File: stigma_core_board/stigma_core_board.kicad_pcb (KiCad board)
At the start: 4 copper layers, 40 x 40 mm, 93 parts, among them J1 TC2050, J5 USB_C_Receptacle_USB2.0, SW1 KMR721NGLFS, SW2 KMR721NGLFS, U1 STM32H743VITx, U10 H3LIS331DL, U11 MS5607/MS5611, U12 LIS3MDL, U13 BMP580/BMP388/LPS22, U2 TPD4E1U06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

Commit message: Update LCSC references
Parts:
- D4: footprint Diode_SMD:D_SOD-123F -> Diode_SMD:D_SOD-123
- U13: value BMP580/BMP388/LPS22 -> BMP580
- U3: value BMP580/BMP388/LPS22 -> LPS22
- U6: value ICM-42688 (or other LGA-14 IMU) -> ICM-42688-P
- moved D4 0.25 mm to (126.2, 109.8)

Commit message: Tweak routing
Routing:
- net GND: track 112.1 -> 124.4 mm, vias 195 -> 202
- net SWDIO: track 12.1 -> 17.4 mm
- net PC1_ETH_MDC: track 8.57 -> 11.6 mm
- net PA3: track 7.15 -> 10.2 mm
- net Net-(J1-Pin_2): track 24.8 -> 27.7 mm
- net PA2_ETH_MDIO: track 9.07 -> 11.2 mm
- net PE2: track 16.9 -> 15.2 mm
- net PA1_ETH_REF_CLK: track 8.57 -> 10.2 mm
- net PA0: track 8.47 -> 9.84 mm
- net PA7_ETH_CRS_DV: track 12.5 -> 11.6 mm
- net PB1: track 15.6 -> 14.7 mm
- net ETH_RXD+: track 11.6 -> 10.9 mm
- net ETH_RXD-: track 11.5 -> 10.8 mm
- net Net-(J5-CC1): track 7.58 -> 8.10 mm

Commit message: Minor layout tweaks
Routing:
- net +5V: track 84.9 -> 85.8 mm
- net PC1_ETH_MDC: track 11.6 -> 10.9 mm
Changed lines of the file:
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@@
 	)
 	(segment
+		(start 113.2 124.85)
+		(end 114.05 124.85)
+		(width 0.5)
+		(layer "F.Cu")
+		(net 11)
+	)
+	(segment
 		(start 125.85 130.95)
 		(end 126.15 130.95)
@@
 	(segment
 		(start 113.2 124.85)
-		(end 114.05 124.85)
-		(width 0.5)
-		(layer "F.Cu")
-		(net 11)
-	)
-	(segment
-		(start 113.2 124.85)
 		(end 112.875 125.175)
 		(width 0.5)
@@
 	)
 	(segment
+		(start 114.05 124.85)
+		(end 113.2 124.85)
+		(width 0.5)
+		(layer "B.Cu")
+		(net 11)
+	)
+	(segment
 		(start 106.45 121.88)
 		(end 106.45 119.3)
@@
 	)
 	(segment
-		(start 108.724999 115.833299)
-		(end 108.682689 115.833299)
+		(start 108.720327 115.795661)
+		(end 108.265988 116.25)
 		(width 0.2)
 		(layer "F.Cu")
@@
 	)
 	(segment
-		(start 108.682689 115.833299)
-		(end 108.265988 116.25)
+		(start 109.062003 115.795661)
+		(end 108.720327 115.795661)
 		(width 0.2)
 		(layer "F.Cu")
@@
 	)
 	(via
-		(at 108.724999 115.833299)
+		(at 109.062003 115.795661)
 		(size 0.5)
 		(drill 0.25)
@@
 	)
 	(segment
-		(start 108.724999 115.833299)
-		(end 109.188305 115.833299)
+		(start 109.150667 115.795661)
+		(end 109.65 116.294994)
 		(width 0.2)
 		(layer "B.Cu")
@@
 	)
 	(segment
-		(start 109.188305 115.833299)
-		(end 109.65 116.294994)
+		(start 109.062003 115.795661)
+		(end 109.150667 115.795661)
 		(width 0.2)
 		(layer "B.Cu")
@@
 	)
 	(via
-		(at 109.15 114.638083)
+		(at 109.14 114.54)
 		(size 0.5)
 		(drill 0.25)
@@
 	)
 	(segment
-		(start 109.15 114.305006)
-		(end 109.25 114.205006)
-		(width 0.2)
-		(layer "B.Cu")
-		(net 88)
-	)
-	(segment
 		(start 112.018146 115.031408)
 		(end 112.05 114.999554)
@@
 	)
 	(segment
-		(start 109.25 114.205006)
-		(end 109.25 113.89)
-		(width 0.2)
-		(layer "B.Cu")
-		(net 88)
-	)
-	(segment
 		(start 118.85 113.4)
 		(end 118.6 113.15)
@@
 	)
 	(segment
-		(start 109.15 114.638083)
-		(end 109.15 114.305006)
+		(start 118.6 113.15)
+		(end 118.25 113.15)
 		(width 0.2)
 		(layer "B.Cu")
@@
 	)
 	(segment
-		(start 118.6 113.15)
-		(end 118.25 113.15)
+		(start 115.25 113.231801)
+		(end 115.25 113.89)
 		(width 0.2)
 		(layer "B.Cu")
@@
 	)
 	(segment
-		(start 115.25 113.231801)
-		(end 115.25 113.89)
+		(start 109.14 114.315006)
+		(end 109.25 114.205006)
 		(width 0.2)
 		(layer "B.Cu")
@@
 	)
 	(segment
+		(start 109.14 114.54)
+		(end 109.14 114.315006)
+		(width 0.2)
+		(layer "B.Cu")
+		(net 88)
+	)
+	(segment
 		(start 111.958462 115.031408)
 		(end 111.613873 114.686819)
@@
 	)
 	(segment
+		(start 109.25 114.205006)
+		(end 109.25 113.89)
+		(width 0.2)
+		(layer "B.Cu")
+		(net 88)
+	)
+	(segment
 		(start 121.25 113.517618)
 		(end 121.25 113.89)
@@
 	)
 	(segment
-		(start 109.6 115.8)
-		(end 109.6 115.901472)
+		(start 108.990736 116.245661)
+		(end 108.486397 116.75)
 		(width 0.2)
 		(layer "F.Cu")
@@
 	)
 	(segment
-		(start 109.48 113.79)
-		(end 108.84 113.79)
+		(start 109.27 115.28)
+		(end 109.48 115.28)
 		(width 0.2)
 		(layer "F.Cu")
@@
 	)
 	(segment
-		(start 108.72 113.91)
-		(end 108.72 113.97)
+		(start 109.48 113.79)
+		(end 108.84 113.79)
 		(width 0.2)
 		(layer "F.Cu")
@@
 	)
 	(segment
-		(start 108.93 115.42)
-		(end 109.48 115.42)
+		(start 108.72 113.91)
+		(end 108.72 113.97)
 		(width 0.2)
 		(layer "F.Cu")
@@
 	)
 	(segment
-		(start 108.486397 116.75)
-		(end 107.575 116.75)
+		(start 108.84 114.09)
+		(end 109.48 114.09)
 		(width 0.2)
 		(layer "F.Cu")
@@
 	)
 	(segment
-		(start 108.84 114.09)
-		(end 109.48 114.09)
+		(start 109.6 113.108828)
+		(end 109.6 113.67)
 		(width 0.2)
 		(layer "F.Cu")
@@
 	)
 	(segment
-		(start 109.6 115.901472)
-		(end 109.255811 116.245661)
+		(start 109.6 114.27)
+		(end 109.6 114.3)
 		(width 0.2)
 		(layer "F.Cu")
@@
 	)
 	(segment
-		(start 109.255811 116.245661)
-		(end 108.990736 116.245661)
+		(start 109.583123 113.091951)
+		(end 109.6 113.108828)
 		(width 0.2)
 		(layer "F.Cu")
@@
 	)
 	(segment
-		(start 109.6 113.108828)
-		(end 109.6 113.67)
+		(start 109.6 115.46)
+		(end 109.6 115.8)
 		(width 0.2)
 		(layer "F.Cu")
@@
 	)
 	(segment
-		(start 109.6 114.3)
-		(end 109.6 115)
+		(start 109.6 115.8)
+		(end 109.6 115.901472)
 		(width 0.2)
 		(layer "F.Cu")
@@
 	)
 	(segment
-		(start 109.6 114.27)
-		(end 109.6 114.3)
+		(start 109.6 114.21)
+		(end 109.6 114.27)
 		(width 0.2)
 		(layer "F.Cu")
@@
 	)
 	(segment
-		(start 109.583123 113.091951)
-		(end 109.6 113.108828)
+		(start 109.6 115.901472)
+		(end 109.255811 116.245661)
 		(width 0.2)
 		(layer "F.Cu")
@@
 	)
 	(segment
-		(start 109.48 115.12)
-		(end 108.93 115.12)
+		(start 109.15 115.1)
+		(end 109.15 115.16)
 		(width 0.2)
 		(layer "F.Cu")
@@
 	)
 	(segment
-		(start 108.990736 116.245661)
-		(end 108.486397 116.75)
+		(start 109.48 114.98)
+		(end 109.27 114.98)
 		(width 0.2)
 		(layer "F.Cu")
@@
 	)
 	(segment
-		(start 109.6 114.21)
-		(end 109.6 114.27)
+		(start 109.6 114.3)
+		(end 109.6 114.86)
 		(width 0.2)
 		(layer "F.Cu")
@@
 	)
 	(segment
-		(start 109.6 115.6)
-		(end 109.6 115.8)
+		(start 109.6 115.4)
+		(end 109.6 115.46)
 		(width 0.2)
 		(layer "F.Cu")
@@
 	)
 	(segment
-		(start 109.6 115.54)
-		(end 109.6 115.6)
+		(start 108.486397 116.75)
+		(end 107.575 116.75)
 		(width 0.2)
 		(layer "F.Cu")
@@
 	)
 	(segment
-		(start 108.81 115.24)
-		(end 108.81 115.3)
+		(start 109.255811 116.245661)
+		(end 108.990736 116.245661)
 		(width 0.2)
 		(layer "F.Cu")
@@
 	)
 	(arc
-		(start 108.81 115.3)
-		(mid 108.845147 115.384853)
-		(end 108.93 115.42)
+		(start 109.6 114.86)
+		(mid 109.564853 114.944853)
+		(end 109.48 114.98)
+		(width 0.2)
+		(layer "F.Cu")
+		(net 125)
+	)
+	(arc
+		(start 109.48 115.28)
+		(mid 109.564853 115.315147)
+		(end 109.6 115.4)
 		(width 0.2)
 		(layer "F.Cu")
@@
 	)
 	(arc
-		(start 108.93 115.12)
-		(mid 108.845147 115.155147)
-		(end 108.81 115.24)
+		(start 109.27 114.98)
+		(mid 109.185147 115.015147)
+		(end 109.15 115.1)
+		(width 0.2)
+		(layer "F.Cu")
+		(net 125)
+	)
+	(arc
+		(start 109.15 115.16)
+		(mid 109.185147 115.244853)
+		(end 109.27 115.28)
 		(width 0.2)
 		(layer "F.Cu")
@@
 		(net 125)
 	)
-	(arc
-		(start 109.6 115)
-		(mid 109.564853 115.084853)
-		(end 109.48 115.12)
-		(width 0.2)
-		(layer "F.Cu")
-		(net 125)
-	)
-	(arc
-		(start 109.48 115.42)
-		(mid 109.564853 115.455147)
-		(end 109.6 115.54)
-		(width 0.2)
-		(layer "F.Cu")
-		(net 125)
-	)
 	(segment
 		(start 109.583123 113.091951)
@@
 		(base_line
 			(pts
-				(xy 109.6 115) (xy 109.6 115.8)
+				(xy 109.6 114.86) (xy 109.6 115.8)
 			)
 		)
@@
 		(last_status "tuned")
 		(last_track_width 0.2)
-		(last_tuning "13.0728 mm (tuned)")
-		(max_amplitude 1.04)
+		(last_tuning "12.5132 mm (tuned)")
+		(max_amplitude 0.6)
 		(min_amplitude 0.02)
 		(min_spacing 0.17)
 		(origin
-			(xy 109.6 115)
+			(xy 109.6 114.86)
 		)
 		(override_custom_rules no)
@@
 		(target_skew_min -0.1)
 		(tuning_mode "single")
-		(members 2585e20f-4a8c-478d-8ac4-1149f265714d 3559a627-c0c3-4b64-b16a-5b7b8ac6a93f
-			80fbf513-ff44-4c1f-84ea-3771d7bc1094 91e31208-cc61-4093-8448-1f3f3987d2a7
-			ba443be0-f628-483e-93a6-540849705d64 cb82639a-6d50-4b85-8166-b86fdd5ead69
-			e418a197-abfd-4e90-8c6e-e574207fe112 e46d68df-d1e5-4b40-bb3c-5f89e9fb42ec
-			e6e14e78-9cec-4210-a722-a0c50c543ec3
+		(members 0259e00c-9ed5-4fd1-8282-a53396e8aba6 21b8111f-1cc3-4966-b26e-453f928ff981
+			36fdd3e3-f6ef-481d-a199-ed1790eb7bd5 74bef20d-ed03-483a-9934-713e3eae4cce
+			898c97ab-6e85-4e9c-91ca-d3bfb0b45b93 9700eba5-da46-4409-999c-fde6f670c7de
+			b0942bd4-7091-4582-a69b-6ab1850de12c b61dd31d-4ab2-4ac4-bc0f-979b543bdf15
+			d03feb0c-e362-4b17-8e16-c53f901778ce
 		)
 	)

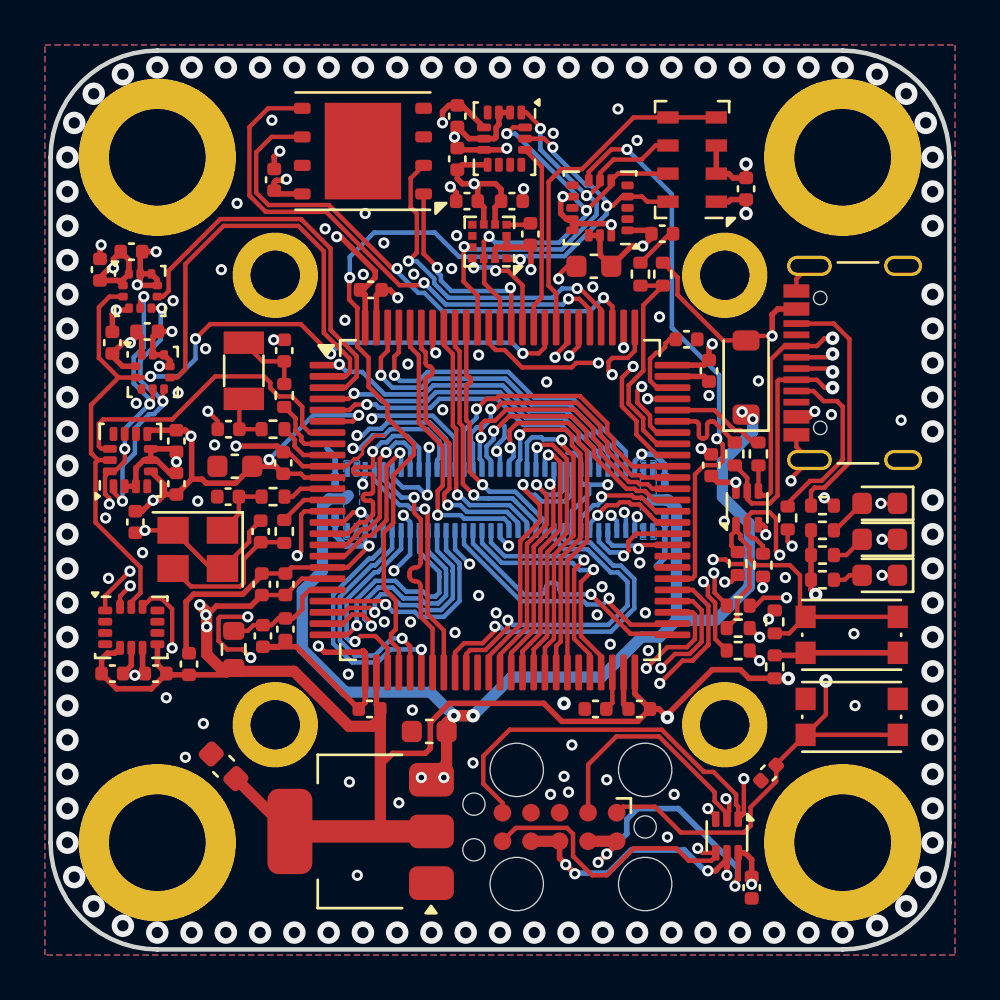
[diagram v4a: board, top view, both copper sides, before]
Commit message: Minor routing tweaks, add net colors
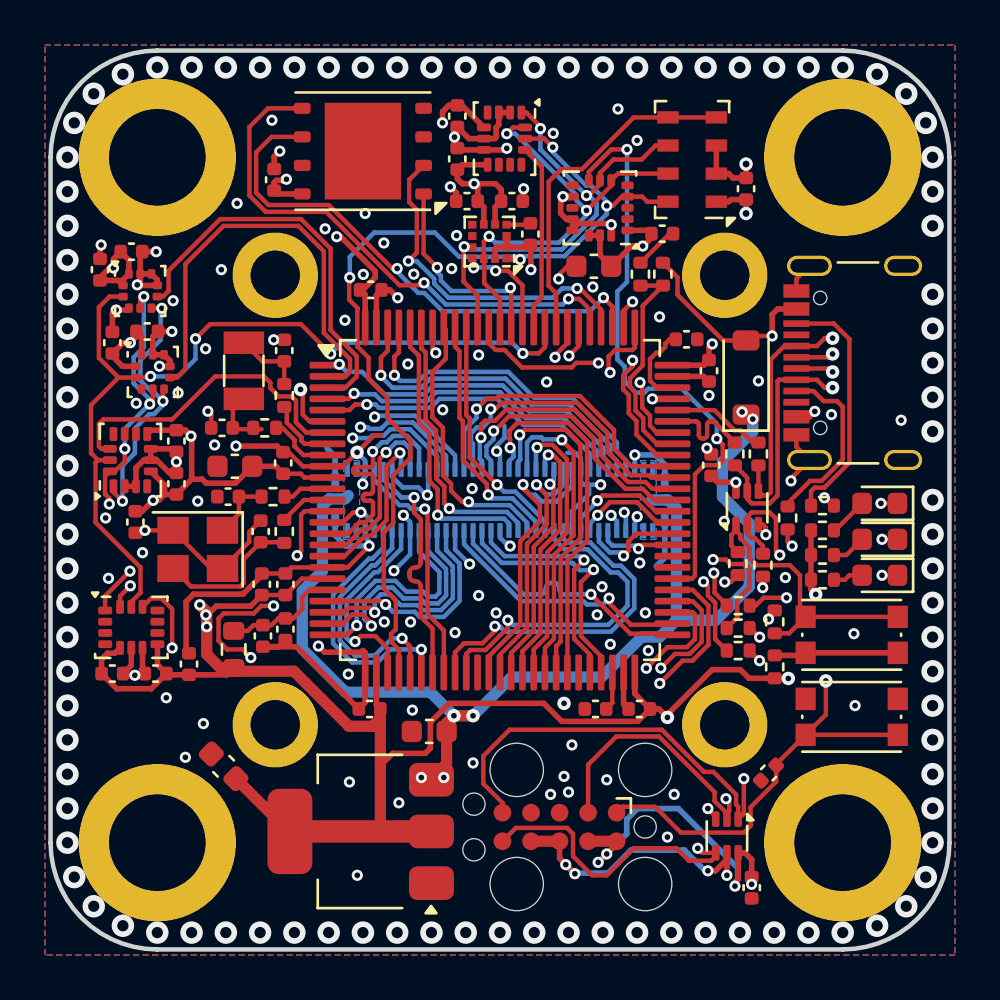
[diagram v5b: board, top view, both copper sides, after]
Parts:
- moved R4 0.37 mm to (104.8, 112.0)
- moved C14 0.30 mm to (102.9, 112.0)
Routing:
- net LED_GREEN: track 26.1 -> 28.1 mm
- net SPI1_CS_HIGHG: track 25.2 -> 27.0 mm
- net SPI3_MOSI: track 45.1 -> 43.9 mm
- net PD1: track 10.9 -> 11.9 mm
- net SPI3_MISO: track 33.8 -> 32.8 mm
- net +3.3V: track 230.4 -> 231.4 mm, vias 23 -> 22
- net GND: track 124.3 -> 123.4 mm, vias 202 -> 203
- net PD0: track 10.5 -> 11.3 mm
- net SPI3_SCK: track 40.3 -> 39.5 mm
- net PB5: track 11.4 -> 10.8 mm
- net PB7: track 11.7 -> 12.2 mm

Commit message: minor changes
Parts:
- U4: value IIM-42652 (or other LGA-14 IMU) -> ICM-42670-P
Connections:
- net Net-(C10-Pad1) renamed /VCAP2
- net Net-(C9-Pad1) renamed /VCAP1
- net Net-(D4-A) renamed /VBUS
- net Net-(J1-Pin_2) renamed /J1-SWDIO
- net Net-(J1-Pin_5) renamed /J1-SWO

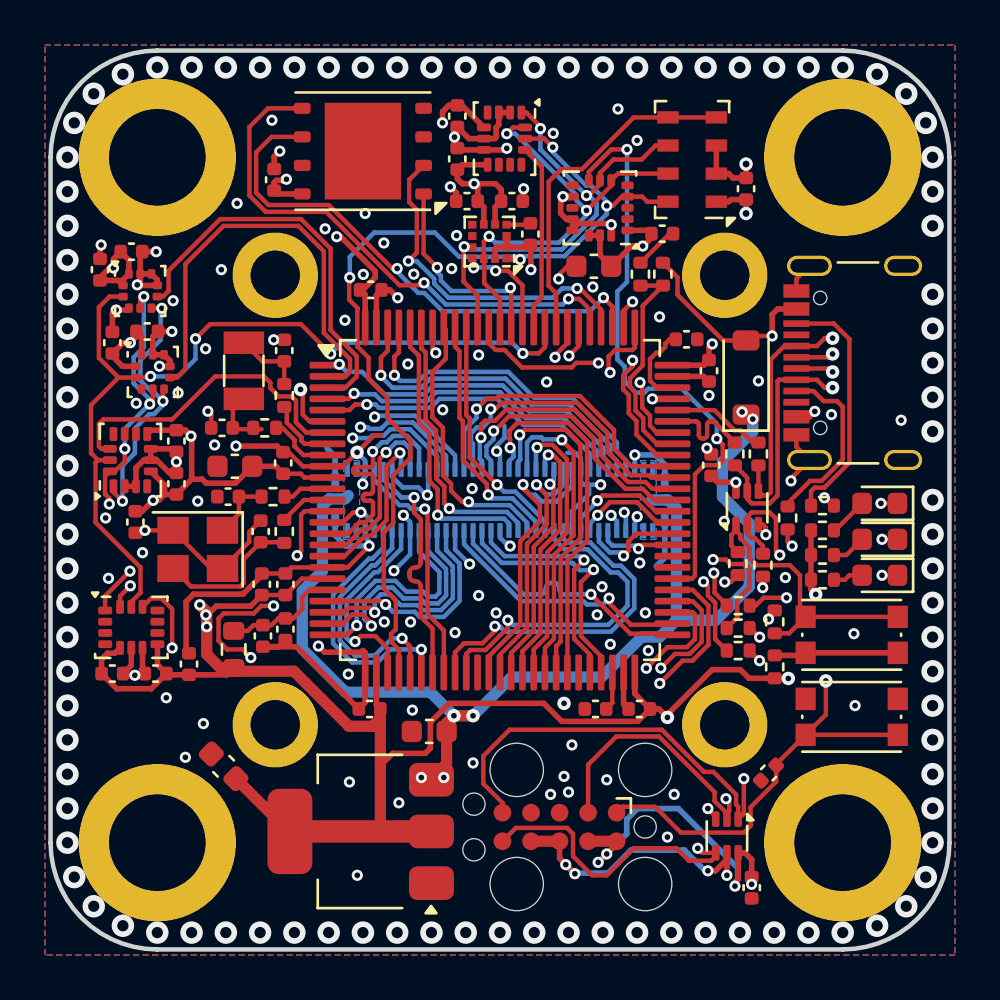
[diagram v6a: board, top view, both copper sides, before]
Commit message: Add correct load capacitors, tweak USB routing, fab options
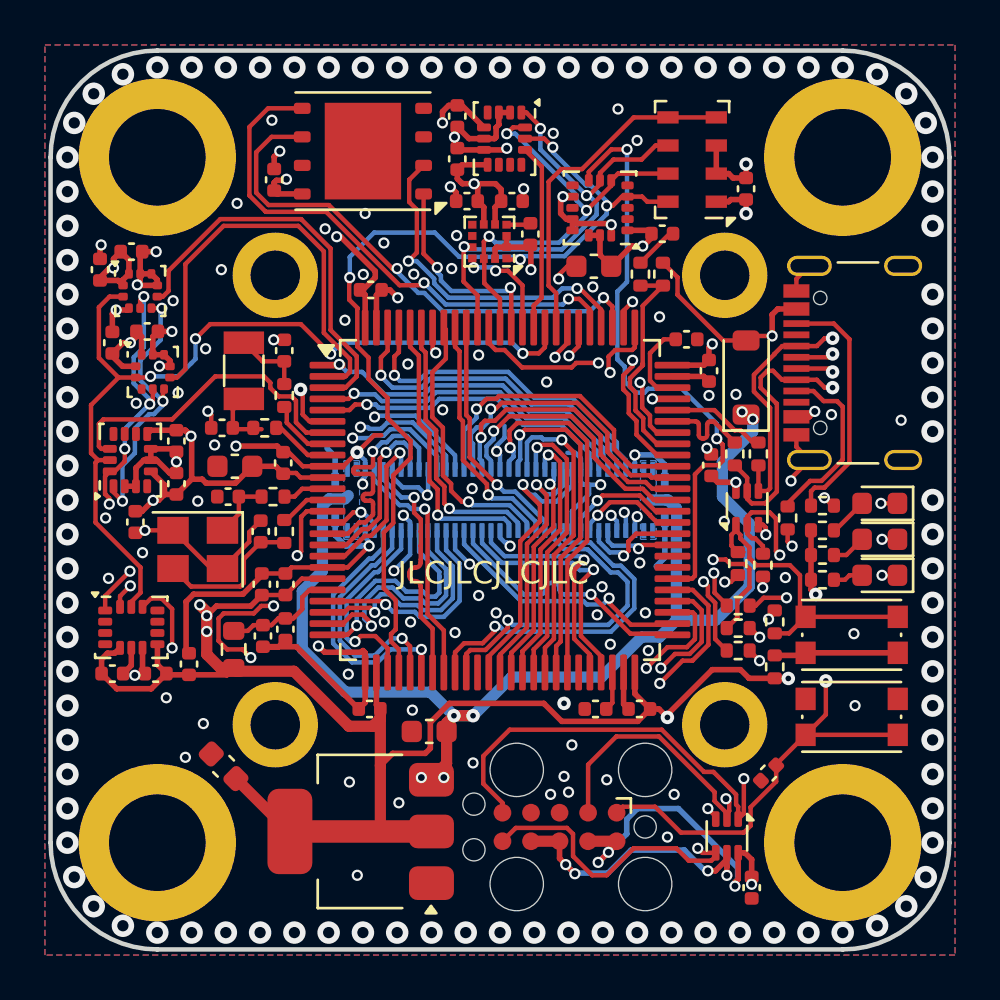
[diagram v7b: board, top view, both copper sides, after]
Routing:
- net /D0-: track 14.6 -> 15.9 mm
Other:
- board text added: "JLCJLCJLCJLC"

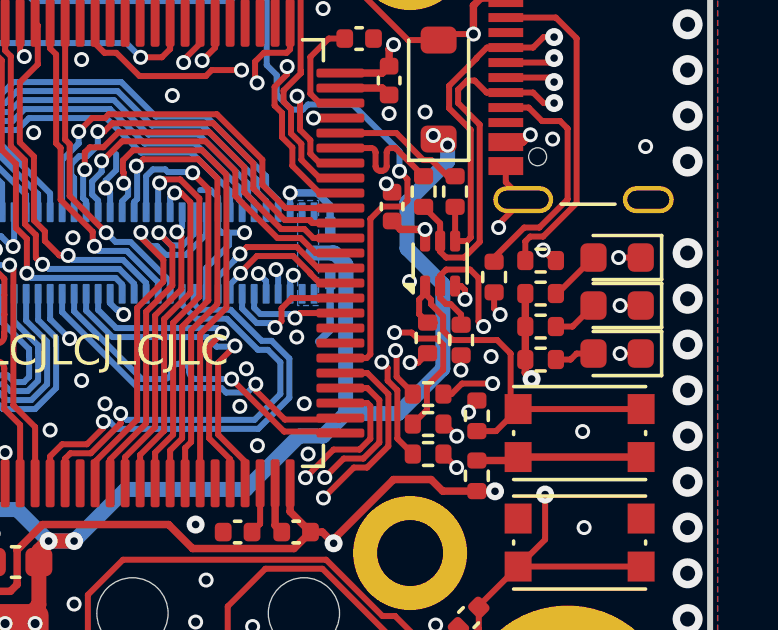
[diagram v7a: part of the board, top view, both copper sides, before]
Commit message: remove rst and boot from USB TSV diode
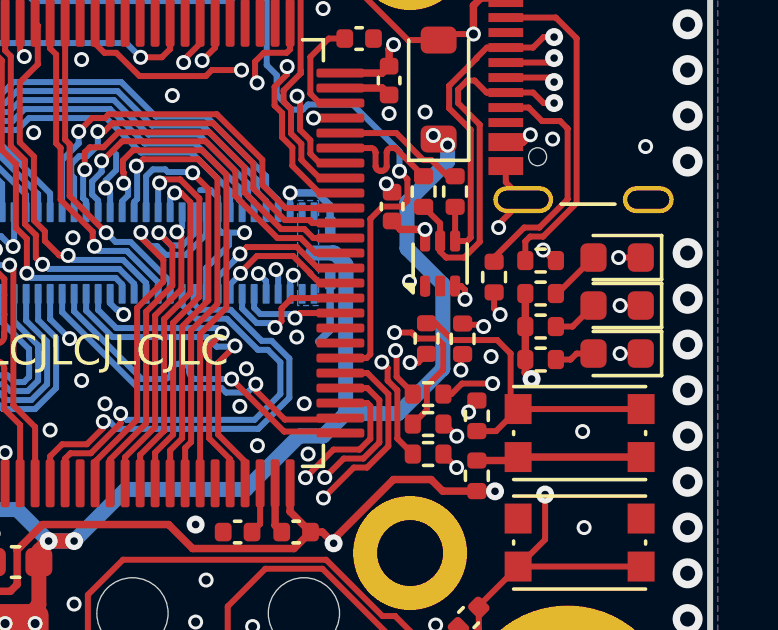
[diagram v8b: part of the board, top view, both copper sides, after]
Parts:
- C11, C12: value 3.9p -> 10p
- C13, C14: value 1.5p -> 10p
- J3: value ~ -> CONN PLUG 70POS SMD GOLD
- R12, R13: value 22 -> 22R
- moved R17 0.06 mm to (127.0, 118.1)
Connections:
- U2 pad 1: BOOT -> unconnected-(U2-IO1-Pad1)
- U2 pad 2: NRST -> unconnected-(U2-IO2-Pad2)
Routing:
- net NRST: track 31.8 -> 27.4 mm
- net BOOT: track 13.7 -> 10.9 mm
- net unconnected-(U2-IO1-Pad1): track 0.00 -> 0.51 mm
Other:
- board text added: "rev 2"
- board text removed: "rev 1"
